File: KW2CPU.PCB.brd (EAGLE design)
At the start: 50 x 30 mm, 66 parts, among them J1 DF12_M, J2 MOLEX55560-0207, J3 MMCX_VERT, U1 MKW21D, U2 AT45DB161D8S1, U3 RF6555, U5 F-ANTENNA, X1 32KHZ, X2 32MHZ

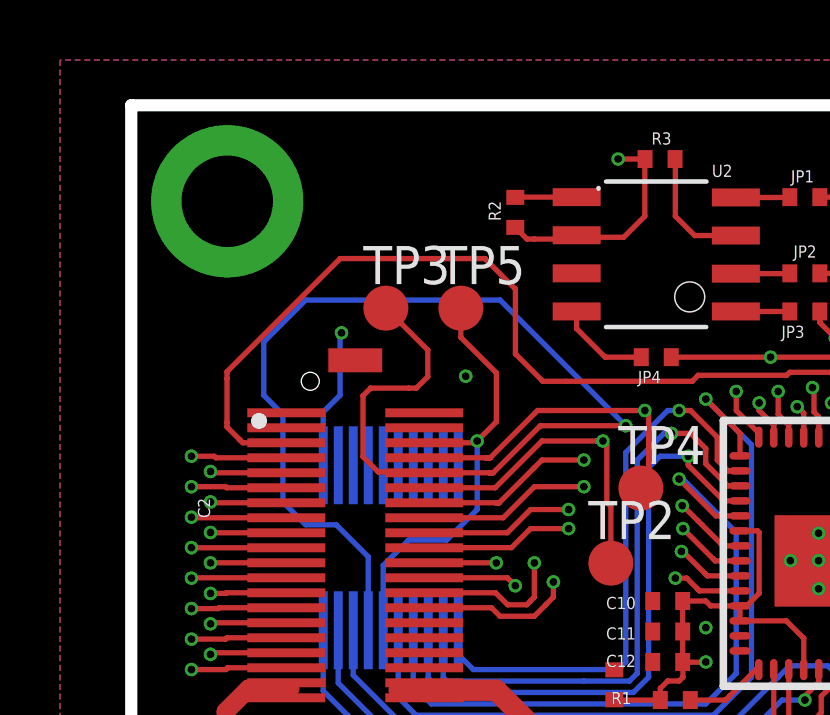
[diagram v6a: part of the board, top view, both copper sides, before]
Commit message: Added timing TPs
For radio calibration. Also exported CAD model
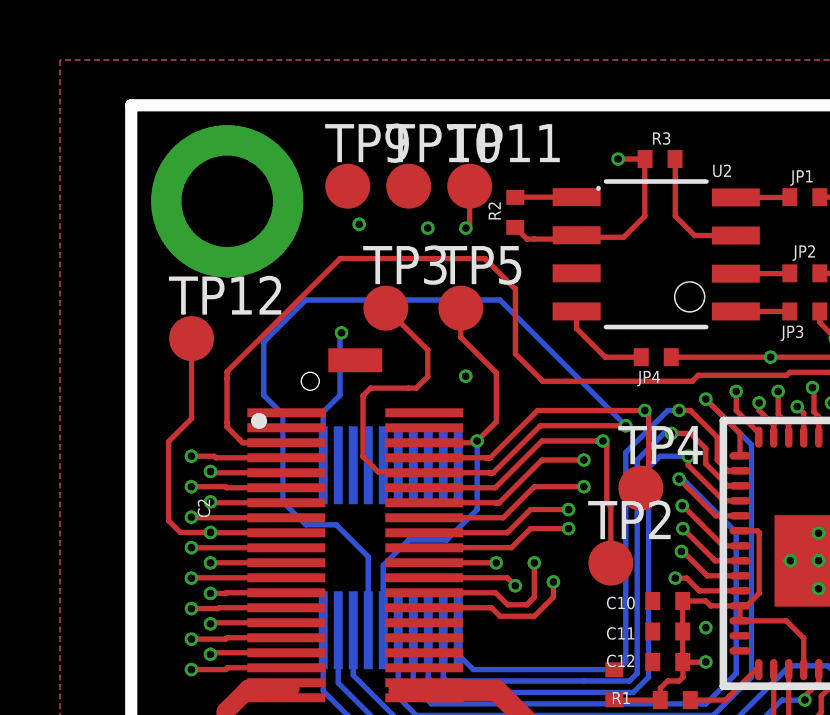
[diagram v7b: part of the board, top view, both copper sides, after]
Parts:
- added TP10, TP11, TP12, TP9: PTR1TP15R, testpad:TP15R
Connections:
- net PTD4/LLWU_P14/MADC0_SE21/SPI0_PCS1/!UART0_RTS!/FTM0_CH4/EWM_IN/GPIO_BSM_FRAME: now also TP9.TP
- net PTD5/ADC0_SE6B/SPI0_PCS2/!UART0_CTS!/!UART0_COL!/FTM0_CH5/!EWM_OUT: now also TP10.TP
- net PTD6/LLWU_P15/ADC0_SE7B/SPI0_PCS3/UART0_RX/FTM0_CH6/FTM0_FLT0: now also TP11.TP
- net PTD7/MADC0_SE22/CMT_IRO/UART0_TX/FTM0_CH7/FTM0_FLT1: now also TP12.TP
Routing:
- net PTD6/LLWU_P15/ADC0_SE7B/SPI0_PCS3/UART0_RX/FTM0_CH6/FTM0_FLT0: track 31.0 -> 49.0 mm, vias 2 -> 3
- net PTD5/ADC0_SE6B/SPI0_PCS2/!UART0_CTS!/!UART0_COL!/FTM0_CH5/!EWM_OUT: track 35.3 -> 50.1 mm, vias 2 -> 3
- net PTD4/LLWU_P14/MADC0_SE21/SPI0_PCS1/!UART0_RTS!/FTM0_CH4/EWM_IN/GPIO_BSM_FRAME: track 38.2 -> 52.0 mm, vias 2 -> 3
- net PTD7/MADC0_SE22/CMT_IRO/UART0_TX/FTM0_CH7/FTM0_FLT1: track 28.9 -> 36.9 mm
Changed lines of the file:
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@@
 <grid distance="5" unitdist="mil" unit="mil" style="lines" multiple="1" display="yes" altdistance="0.000123031496" altunitdist="mil" altunit="mil"/>
 <layers>
-<layer number="1" name="Top" color="4" fill="1" visible="yes" active="yes"/>
+<layer number="1" name="Top" color="4" fill="1" visible="no" active="yes"/>
 <layer number="2" name="Route2" color="11" fill="1" visible="no" active="yes"/>
-<layer number="3" name="Route3" color="10" fill="1" visible="no" active="yes"/>
+<layer number="3" name="Route3" color="10" fill="1" visible="yes" active="yes"/>
 <layer number="4" name="Route4" color="1" fill="4" visible="no" active="no"/>
 <layer number="5" name="Route5" color="4" fill="4" visible="no" active="no"/>
@@
 <attribute name="TP_SIGNAL_NAME" value="" x="27" y="10.5" size="1.778" layer="27" display="off"/>
 </element>
+<element name="TP9" library="testpad" package="TP15R" value="PTR1TP15R" x="-1.27" y="12.065">
+<attribute name="TP_SIGNAL_NAME" value="" x="-1.27" y="12.065" size="1.778" layer="27" display="off"/>
+</element>
+<element name="TP10" library="testpad" package="TP15R" value="PTR1TP15R" x="0.762" y="12.065">
+<attribute name="TP_SIGNAL_NAME" value="" x="0.762" y="12.065" size="1.778" layer="27" display="off"/>
+</element>
+<element name="TP11" library="testpad" package="TP15R" value="PTR1TP15R" x="2.794" y="12.065">
+<attribute name="TP_SIGNAL_NAME" value="" x="2.794" y="12.065" size="1.778" layer="27" display="off"/>
+</element>
+<element name="TP12" library="testpad" package="TP15R" value="PTR1TP15R" x="-6.477" y="6.985">
+<attribute name="TP_SIGNAL_NAME" value="" x="-6.477" y="6.985" size="1.778" layer="27" display="off"/>
+</element>
 </elements>
 <signals>
@@
 <wire x1="13.93" y1="3.701" x2="13.93" y2="4.497" width="0.1778" layer="1"/>
 <wire x1="13.93" y1="4.497" x2="13.712" y2="4.715" width="0.1778" layer="1"/>
+<contactref element="TP9" pad="TP"/>
+<via x="-0.889" y="10.795" extent="1-16" drill="0.254"/>
+<wire x1="-0.889" y1="10.795" x2="-0.889" y2="6.35" width="0.1778" layer="3"/>
+<wire x1="-0.889" y1="6.35" x2="-1.143" y2="6.096" width="0.1778" layer="3"/>
+<wire x1="-1.143" y1="6.096" x2="-1.143" y2="2.667" width="0.1778" layer="3"/>
+<wire x1="-1.143" y1="2.667" x2="-1.778" y2="2.032" width="0.1778" layer="3"/>
+<wire x1="-1.778" y1="2.032" x2="-6.465" y2="2.032" width="0.1778" layer="3"/>
+<wire x1="-6.465" y1="2.032" x2="-6.481" y2="2.048" width="0.1778" layer="3"/>
+<wire x1="-0.889" y1="10.795" x2="-1.27" y2="12.065" width="0" layer="19" extent="1-1"/>
 </signal>
 <signal name="PTD5/ADC0_SE6B/SPI0_PCS2/!UART0_CTS!/!UART0_COL!/FTM0_CH5/!EWM_OUT">
@@
 <wire x1="13.43" y1="3.701" x2="13.43" y2="4.108" width="0.1778" layer="1"/>
 <wire x1="13.43" y1="4.108" x2="13.077" y2="4.461" width="0.1778" layer="1"/>
+<contactref element="TP10" pad="TP"/>
+<via x="1.397" y="10.668" extent="1-16" drill="0.254"/>
+<wire x1="1.397" y1="10.668" x2="1.397" y2="4.318" width="0.1778" layer="3"/>
+<wire x1="1.397" y1="4.318" x2="-1.397" y2="1.524" width="0.1778" layer="3"/>
+<wire x1="-1.397" y1="1.524" x2="-5.83" y2="1.524" width="0.1778" layer="3"/>
+<wire x1="-5.83" y1="1.524" x2="-5.846" y2="1.54" width="0.1778" layer="3"/>
+<wire x1="1.397" y1="10.668" x2="0.762" y2="12.065" width="0" layer="19" extent="1-1"/>
 </signal>
 <signal name="PTD6/LLWU_P15/ADC0_SE7B/SPI0_PCS3/UART0_RX/FTM0_CH6/FTM0_FLT0">
@@
 <wire x1="12.93" y1="3.701" x2="12.93" y2="4.1" width="0.1778" layer="1"/>
 <wire x1="12.93" y1="4.1" x2="12.442" y2="4.588" width="0.1778" layer="1"/>
+<contactref element="TP11" pad="TP"/>
+<wire x1="2.794" y1="12.065" x2="2.794" y2="10.795" width="0.1778" layer="1"/>
+<wire x1="2.794" y1="10.795" x2="2.667" y2="10.668" width="0.1778" layer="1"/>
+<via x="2.667" y="10.668" extent="1-16" drill="0.254"/>
+<wire x1="2.667" y1="10.668" x2="2.667" y2="7.493" width="0.1778" layer="3"/>
+<wire x1="2.032" y1="4.191" x2="1.778" y2="3.937" width="0.1778" layer="3"/>
+<wire x1="1.778" y1="3.937" x2="-1.143" y2="1.016" width="0.1778" layer="3"/>
+<wire x1="-1.143" y1="1.016" x2="-6.465" y2="1.016" width="0.1778" layer="3"/>
+<wire x1="-6.465" y1="1.016" x2="-6.481" y2="1.032" width="0.1778" layer="3"/>
+<wire x1="2.667" y1="7.493" x2="2.667" y2="6.858" width="0.1778" layer="3"/>
+<wire x1="2.667" y1="6.858" x2="2.032" y2="6.223" width="0.1778" layer="3"/>
+<wire x1="2.032" y1="6.223" x2="2.032" y2="4.191" width="0.1778" layer="3"/>
 </signal>
 <signal name="PTD7/MADC0_SE22/CMT_IRO/UART0_TX/FTM0_CH7/FTM0_FLT1">
@@
 <wire x1="12.43" y1="3.701" x2="12.43" y2="3.838" width="0.1778" layer="1"/>
 <wire x1="12.43" y1="3.838" x2="11.68" y2="4.588" width="0.1778" layer="1"/>
+<contactref element="TP12" pad="TP"/>
+<wire x1="-6.477" y1="6.985" x2="-6.477" y2="4.318" width="0.1778" layer="1"/>
+<wire x1="-6.477" y1="4.318" x2="-7.239" y2="3.556" width="0.1778" layer="1"/>
+<wire x1="-7.239" y1="3.556" x2="-7.239" y2="0.912084375" width="0.1778" layer="1"/>
+<wire x1="-7.239" y1="0.912084375" x2="-6.848875" y2="0.521959375" width="0.1778" layer="1"/>
+<wire x1="-6.848875" y1="0.521959375" x2="-5.848040625" y2="0.521959375" width="0.1778" layer="1"/>
+<wire x1="-5.848040625" y1="0.521959375" x2="-5.846" y2="0.524" width="0.1778" layer="1"/>
 </signal>
 <signal name="PTE0/MADC0_SE10/SPI1_PCS1/UART1_TX/MTRACE_CLKOUT/I2C1_SDA/RTC_CLKOUT">

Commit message: Fixed PTC5 label and added RESET pullup
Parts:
- added R10: 10K, GW-devices:RF-R0402
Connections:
- net !RESET: now also R10.1
- net +3V3: now also R10.2
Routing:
- net PTD5/ADC0_SE6B/SPI0_PCS2/!UART0_CTS!/!UART0_COL!/FTM0_CH5/!EWM_OUT: track 50.1 -> 51.7 mm
- net PTD4/LLWU_P14/MADC0_SE21/SPI0_PCS1/!UART0_RTS!/FTM0_CH4/EWM_IN/GPIO_BSM_FRAME: track 52.0 -> 53.4 mm
- net +3V3: track 57.7 -> 59.1 mm, vias 13 -> 14
- net PTD1/ADC0_SE5B/SPI0_SCK/!UART2_CTS: track 32.4 -> 31.5 mm
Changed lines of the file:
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@@
 <grid distance="5" unitdist="mil" unit="mil" style="lines" multiple="1" display="yes" altdistance="0.000123031496" altunitdist="mil" altunit="mil"/>
 <layers>
-<layer number="1" name="Top" color="4" fill="1" visible="no" active="yes"/>
-<layer number="2" name="Route2" color="11" fill="1" visible="no" active="yes"/>
+<layer number="1" name="Top" color="4" fill="1" visible="yes" active="yes"/>
+<layer number="2" name="Route2" color="11" fill="1" visible="yes" active="yes"/>
 <layer number="3" name="Route3" color="10" fill="1" visible="yes" active="yes"/>
 <layer number="4" name="Route4" color="1" fill="4" visible="no" active="no"/>
@@
 <layer number="14" name="Route14" color="1" fill="6" visible="no" active="no"/>
 <layer number="15" name="Route15" color="4" fill="6" visible="no" active="no"/>
-<layer number="16" name="Bottom" color="1" fill="1" visible="no" active="yes"/>
+<layer number="16" name="Bottom" color="1" fill="1" visible="yes" active="yes"/>
 <layer number="17" name="Pads" color="2" fill="1" visible="yes" active="yes"/>
 <layer number="18" name="Vias" color="2" fill="1" visible="yes" active="yes"/>
@@
 <rectangle x1="29.90428125" y1="3.02408125" x2="30.3056" y2="3.4254" layer="255"/>
 <rectangle x1="29.90428125" y1="-0.534459375" x2="30.3056" y2="-0.214421875" layer="255"/>
-<rectangle x1="29.90428125" y1="1.624540625" x2="30.3056" y2="1.944578125" layer="255"/>
+<rectangle x1="29.77728125" y1="1.624540625" x2="30.1786" y2="1.944578125" layer="255"/>
 <rectangle x1="29.90428125" y1="0.184359375" x2="30.3056" y2="0.504396875" layer="255"/>
 <rectangle x1="29.90428125" y1="0.90571875" x2="30.3056" y2="1.22575625" layer="255"/>
@@
 <attribute name="TP_SIGNAL_NAME" value="" x="-6.477" y="6.985" size="1.778" layer="27" display="off"/>
 </element>
+<element name="R10" library="GW-devices" package="RF-R0402" value="10K" x="4.191" y="5.207"/>
 </elements>
 <signals>
@@
 <wire x1="19.794" y1="-3.794" x2="20.5" y2="-4.5" width="0.1778" layer="1"/>
 <wire x1="20.5" y1="-4.5" x2="21.975" y2="-4.5" width="0.1778" layer="1"/>
+<contactref element="R10" pad="2"/>
+<wire x1="4.691" y1="5.207" x2="4.572" y2="5.207" width="0.1778" layer="1"/>
+<wire x1="4.572" y1="5.207" x2="4.572" y2="6.35" width="0.1778" layer="1"/>
+<via x="4.572" y="6.477" extent="1-16" drill="0.254"/>
+<wire x1="4.572" y1="6.35" x2="4.572" y2="6.477" width="0.1778" layer="1"/>
 </signal>
 <signal name="EXTAL_32M">
@@
 <wire x1="13.362" y1="5.762" x2="10.412" y2="5.762" width="0.1778" layer="1"/>
 <wire x1="10.412" y1="5.762" x2="10.212" y2="5.562" width="0.1778" layer="1"/>
-<wire x1="10.212" y1="5.562" x2="6.012" y2="5.562" width="0.1778" layer="1"/>
+<wire x1="10.212" y1="5.562" x2="7.917" y2="5.562" width="0.1778" layer="1"/>
 <wire x1="-5.296" y1="5.654" x2="-5.296" y2="4.189" width="0.1778" layer="1"/>
 <wire x1="-2.188" y1="3.512" x2="-3.32" y2="3.512" width="0.1778" layer="1"/>
@@
 <wire x1="-5.296" y1="5.88" x2="-1.524" y2="9.652" width="0.1778" layer="1"/>
 <wire x1="-1.524" y1="9.652" x2="3.302" y2="9.652" width="0.1778" layer="1"/>
-<wire x1="3.302" y1="9.652" x2="4.318" y2="8.636" width="0.1778" layer="1"/>
-<wire x1="4.318" y1="8.636" x2="4.318" y2="6.477" width="0.1778" layer="1"/>
-<wire x1="4.318" y1="6.477" x2="5.207" y2="5.588" width="0.1778" layer="1"/>
-<wire x1="6.012" y1="5.562" x2="5.233" y2="5.562" width="0.1778" layer="1"/>
-<wire x1="5.233" y1="5.562" x2="5.207" y2="5.588" width="0.1778" layer="1"/>
+<wire x1="5.842" y1="6.477" x2="4.572" y2="7.747" width="0.1778" layer="1"/>
+<wire x1="4.572" y1="7.747" x2="4.572" y2="8.382" width="0.1778" layer="1"/>
+<wire x1="4.572" y1="8.382" x2="3.302" y2="9.652" width="0.1778" layer="1"/>
+<wire x1="5.842" y1="6.477" x2="6.477" y2="6.477" width="0.1778" layer="1"/>
+<wire x1="6.477" y1="6.477" x2="7.366" y2="5.588" width="0.1778" layer="1"/>
+<wire x1="7.917" y1="5.562" x2="7.392" y2="5.562" width="0.1778" layer="1"/>
+<wire x1="7.392" y1="5.562" x2="7.366" y2="5.588" width="0.1778" layer="1"/>
 </signal>
 <signal name="PTD2/LLWU_P13/SPI0_SOUT/UART2_RX/I2C0_SDA/GPIO4_BSM_DATA">
@@
 <wire x1="13.93" y1="4.497" x2="13.712" y2="4.715" width="0.1778" layer="1"/>
 <contactref element="TP9" pad="TP"/>
-<via x="-0.889" y="10.795" extent="1-16" drill="0.254"/>
-<wire x1="-0.889" y1="10.795" x2="-0.889" y2="6.35" width="0.1778" layer="3"/>
+<via x="-0.889" y="10.922" extent="1-16" drill="0.254"/>
+<wire x1="-0.889" y1="10.922" x2="-0.889" y2="6.35" width="0.1778" layer="3"/>
 <wire x1="-0.889" y1="6.35" x2="-1.143" y2="6.096" width="0.1778" layer="3"/>
 <wire x1="-1.143" y1="6.096" x2="-1.143" y2="2.667" width="0.1778" layer="3"/>
@@
 <wire x1="-1.778" y1="2.032" x2="-6.465" y2="2.032" width="0.1778" layer="3"/>
 <wire x1="-6.465" y1="2.032" x2="-6.481" y2="2.048" width="0.1778" layer="3"/>
-<wire x1="-0.889" y1="10.795" x2="-1.27" y2="12.065" width="0" layer="19" extent="1-1"/>
+<wire x1="-0.889" y1="10.922" x2="-0.889" y2="11.684" width="0.1778" layer="1"/>
+<wire x1="-0.889" y1="11.684" x2="-1.143" y2="11.938" width="0.1778" layer="1"/>
+<wire x1="-1.143" y1="11.938" x2="-1.27" y2="12.065" width="0.1778" layer="1"/>
 </signal>
 <signal name="PTD5/ADC0_SE6B/SPI0_PCS2/!UART0_CTS!/!UART0_COL!/FTM0_CH5/!EWM_OUT">
@@
 <wire x1="13.43" y1="4.108" x2="13.077" y2="4.461" width="0.1778" layer="1"/>
 <contactref element="TP10" pad="TP"/>
-<via x="1.397" y="10.668" extent="1-16" drill="0.254"/>
-<wire x1="1.397" y1="10.668" x2="1.397" y2="4.318" width="0.1778" layer="3"/>
+<via x="1.397" y="10.922" extent="1-16" drill="0.254"/>
+<wire x1="1.397" y1="10.922" x2="1.397" y2="4.318" width="0.1778" layer="3"/>
 <wire x1="1.397" y1="4.318" x2="-1.397" y2="1.524" width="0.1778" layer="3"/>
 <wire x1="-1.397" y1="1.524" x2="-5.83" y2="1.524" width="0.1778" layer="3"/>
 <wire x1="-5.83" y1="1.524" x2="-5.846" y2="1.54" width="0.1778" layer="3"/>
-<wire x1="1.397" y1="10.668" x2="0.762" y2="12.065" width="0" layer="19" extent="1-1"/>
+<wire x1="1.397" y1="10.922" x2="1.397" y2="11.43" width="0.1778" layer="1"/>
+<wire x1="1.397" y1="11.43" x2="0.762" y2="12.065" width="0.1778" layer="1"/>
 </signal>
 <signal name="PTD6/LLWU_P15/ADC0_SE7B/SPI0_PCS3/UART0_RX/FTM0_CH6/FTM0_FLT0">
@@
 <wire x1="12.93" y1="4.1" x2="12.442" y2="4.588" width="0.1778" layer="1"/>
 <contactref element="TP11" pad="TP"/>
-<wire x1="2.794" y1="12.065" x2="2.794" y2="10.795" width="0.1778" layer="1"/>
-<wire x1="2.794" y1="10.795" x2="2.667" y2="10.668" width="0.1778" layer="1"/>
-<via x="2.667" y="10.668" extent="1-16" drill="0.254"/>
-<wire x1="2.667" y1="10.668" x2="2.667" y2="7.493" width="0.1778" layer="3"/>
+<wire x1="2.794" y1="12.065" x2="2.794" y2="11.049" width="0.1778" layer="1"/>
+<wire x1="2.794" y1="11.049" x2="2.667" y2="10.922" width="0.1778" layer="1"/>
+<via x="2.667" y="10.922" extent="1-16" drill="0.254"/>
+<wire x1="2.667" y1="10.922" x2="2.667" y2="7.493" width="0.1778" layer="3"/>
 <wire x1="2.032" y1="4.191" x2="1.778" y2="3.937" width="0.1778" layer="3"/>
 <wire x1="1.778" y1="3.937" x2="-1.143" y2="1.016" width="0.1778" layer="3"/>
@@
 <wire x1="2.5" y1="8" x2="2.5" y2="7.025" width="0.1778" layer="1"/>
 <wire x1="2.5" y1="7.025" x2="3.683" y2="5.842" width="0.1778" layer="1"/>
-<wire x1="3.683" y1="5.842" x2="3.683" y2="4.211" width="0.1778" layer="1"/>
+<wire x1="3.683" y1="5.842" x2="3.683" y2="5.334" width="0.1778" layer="1"/>
+<wire x1="3.683" y1="5.334" x2="3.683" y2="4.211" width="0.1778" layer="1"/>
 <wire x1="3.683" y1="4.211" x2="3.044" y2="3.572" width="0.1778" layer="1"/>
+<contactref element="R10" pad="1"/>
+<wire x1="3.691" y1="5.207" x2="3.683" y2="5.207" width="0.1778" layer="1"/>
+<wire x1="3.683" y1="5.207" x2="3.683" y2="5.334" width="0.1778" layer="1"/>
 </signal>
 <signal name="VIN">
